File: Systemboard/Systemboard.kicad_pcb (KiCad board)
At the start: 2 copper layers, 194 parts, among them J1 Conn_01x60, J108 Prog BT, J2 Conn_01x02, J3 Conn_01x01, J4 Conn_01x01, J5 PTV112-4420A-A503, Q1 MMBT5551L, Q2 MMBT5551L, Q3 MMBT5551L, Q4 MMBT5551L, Q5 MMBT5551L, U1 INA226, U10 74HC595, U101 ESP32-WROOM-32E, U102 74HC14, U103 TLV73333PDBV, U104 PCM2706CPJTR, U2 LM358, U201 TLV73333PDBV, U202 PCM5102A, U3 J104D2C12VDC.15S, U301 TLV73333PDBV, U4 J104D2C12VDC.15S, U401 74HC14, U5 LM2596S-5, U501 TPA3118D2DAPR, U6 LM2596S-3.3, U7 LM2596S-5, U8 LM2596S-ADJ, U9 LTV-817S, Y101 CSTNE12M0G55A000R0

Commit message: prep board
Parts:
- added REF**: MountingHole_3.2mm_M3, MountingHole:MountingHole_3.2mm_M3, F.Cu at (328.0, 214.0)
- added REF**: MountingHole_3.2mm_M3, MountingHole:MountingHole_3.2mm_M3, F.Cu at (328.0, 254.0)
- moved U501 226.6 mm to (328.0, 234.0)

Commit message: place amp parts
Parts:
- moved Speaker_Front1 376.1 mm to (398.0, 225.6), turned to 90 degrees
- moved Speaker_Rear1 369.3 mm to (392.5, 225.6), turned to 90 degrees
- moved R3 298.8 mm to (388.0, 226.7), turned to -90 degrees
- moved R5 294.9 mm to (388.0, 221.2), turned to -90 degrees
- moved R4 294.1 mm to (388.0, 215.7), turned to -90 degrees
- moved C14 294.0 mm to (385.0, 227.7), turned to 180 degrees
- moved R6 290.8 mm to (388.0, 210.2), turned to -90 degrees
- moved C16 289.8 mm to (385.0, 222.2), turned to 180 degrees
- moved C10 289.5 mm to (376.5, 228.5), turned to -90 degrees
- moved C15 288.6 mm to (385.0, 216.7), turned to 180 degrees
- moved L1 287.5 mm to (370.0, 213.5)
- moved L2 287.3 mm to (370.0, 220.5)
- moved C17 284.8 mm to (385.0, 211.2), turned to 180 degrees
- moved C12 284.7 mm to (376.5, 221.5), turned to -90 degrees
- moved L501 284.6 mm to (370.1, 227.5)
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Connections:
- Speaker_Front1 pad 1: /Speaker_PL -> /Speaker_NL
- Speaker_Front1 pad 2: /Speaker_NL -> /Speaker_PL
- Speaker_Front1 pad 3: /Speaker_PR -> /Speaker_NR
- Speaker_Front1 pad 4: /Speaker_NR -> /Speaker_PR
- Speaker_Rear1 pad 1: /Speaker_PL -> /Speaker_NL
- Speaker_Rear1 pad 2: /Speaker_NL -> /Speaker_PL
- Speaker_Rear1 pad 3: /Speaker_PR -> /Speaker_NR
- Speaker_Rear1 pad 4: /Speaker_NR -> /Speaker_PR

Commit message: user save
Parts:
- removed REF** (x2): MountingHole_3.2mm_M3, MountingHole:MountingHole_3.2mm_M3
- removed U102, U401: 74HC14, Package_SO:SOIC-14_3.9x8.7mm_P1.27mm
- added U11: 74HC14, Package_SO:SOIC-14_3.9x8.7mm_P1.27mm, F.Cu at (143.7, 152.3)
- moved U9 440.9 mm to (489.5, 173.5), turned to -90 degrees
- moved L8 430.1 mm to (478.0, 191.0)
- moved R147 422.2 mm to (492.0, 183.6), turned to 90 degrees
- moved R139 420.4 mm to (489.6, 181.0)
- moved R140 420.4 mm to (489.6, 182.5), turned to 180 degrees
- moved R141 419.5 mm to (490.0, 166.5), turned to 180 degrees
- moved R146 417.6 mm to (487.1, 185.9), turned to 90 degrees
- moved L5 417.1 mm to (466.0, 84.5)
- moved U8 409.8 mm to (478.0, 172.6), turned to 90 degrees
- moved D4 404.8 mm to (467.0, 193.5), turned to -90 degrees
- moved C32 404.7 mm to (490.5, 191.8), turned to -90 degrees
- moved U6 400.1 mm to (466.0, 65.6), turned to 90 degrees
- moved Q4 399.0 mm to (490.0, 186.0)
- moved D2 395.9 mm to (455.5, 87.0), turned to -90 degrees
- moved R148 393.0 mm to (439.2, 17.0), turned to 180 degrees
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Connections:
- C111 pad 1: Net-(U104-VDD) -> /USB DAC/USB_DAC_3V3
- U104 pad 21: Net-(U104-VDD) -> /USB DAC/USB_DAC_3V3

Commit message: Update Systemboard.kicad_pcb
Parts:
- moved C401 312.0 mm to (388.4, -16.3)
- moved C106 310.2 mm to (390.7, -12.2)
- moved R113 308.0 mm to (390.1, -14.2), turned to 180 degrees
- moved C105 306.5 mm to (391.0, -7.62)
- moved R111 304.8 mm to (390.3, -10.2)
- moved R109 301.4 mm to (390.6, -5.59)
- moved C102 295.7 mm to (378.8, -16.0), turned to 180 degrees
- moved C103 295.3 mm to (378.8, -12.2), turned to 180 degrees
- moved C104 294.8 mm to (378.8, -8.38), turned to 180 degrees
- moved R104 293.2 mm to (379.2, -14.0), turned to 180 degrees
- moved R105 292.2 mm to (379.2, -10.2), turned to 180 degrees
- moved R107 291.2 mm to (379.2, -6.35), turned to 180 degrees
- moved U11 290.7 mm to (384.8, -10.2)
- moved J3 283.8 mm to (353.6, -38.4)
- moved J4 280.9 mm to (353.6, -25.4)
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
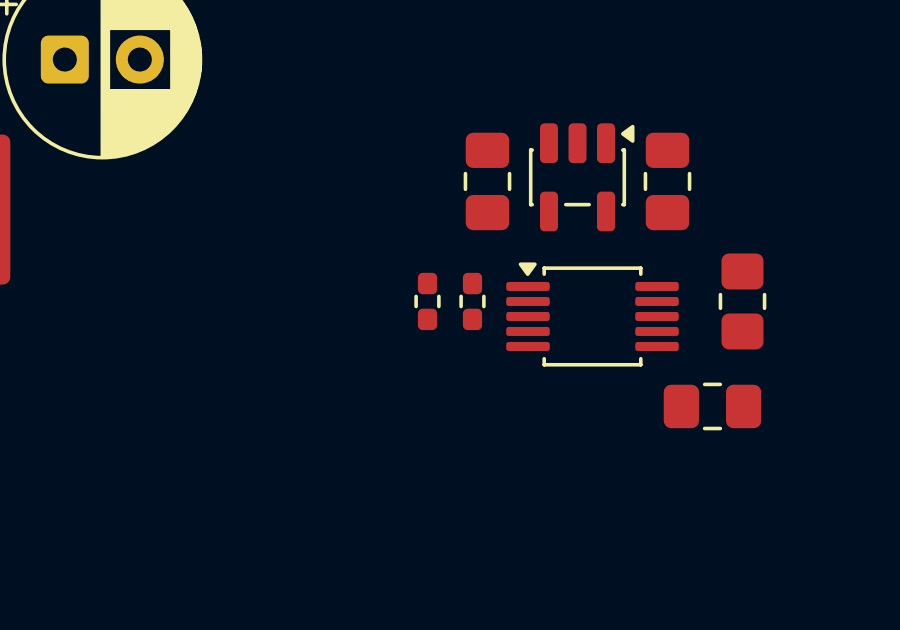
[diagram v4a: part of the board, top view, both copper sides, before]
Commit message: 10k i2c rp down to 4k7
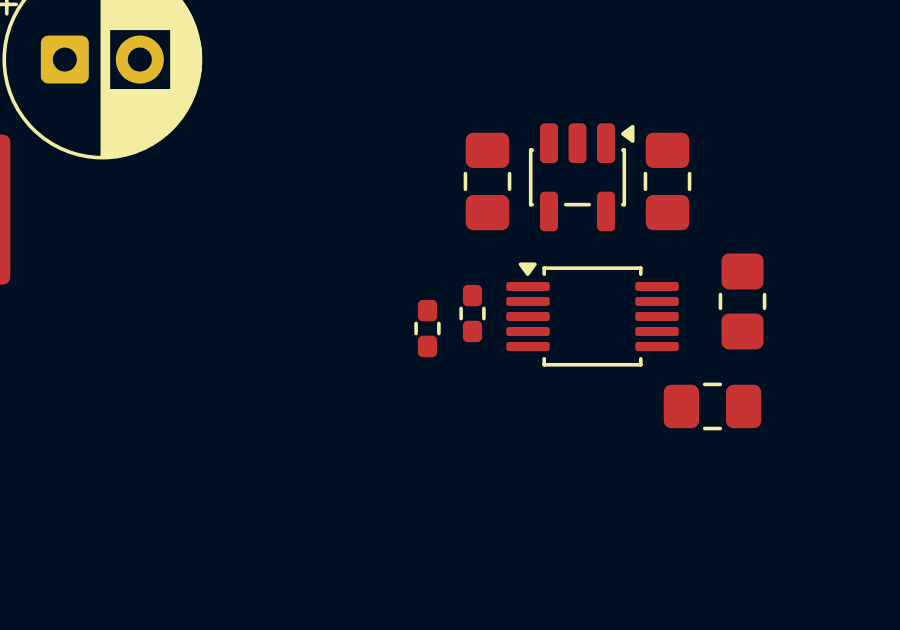
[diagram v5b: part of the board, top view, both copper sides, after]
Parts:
- removed R301, R302: 10k, Resistor_SMD:R_0402_1005Metric_Pad0.72x0.64mm_HandSolder
- added R154: 4k7, Resistor_SMD:R_0402_1005Metric_Pad0.72x0.64mm_HandSolder, F.Cu at (358.0, 67.9)
- added R155: 4k7, Resistor_SMD:R_0402_1005Metric_Pad0.72x0.64mm_HandSolder, F.Cu at (359.5, 67.4)
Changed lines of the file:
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@@
 		)
 	)
+	(footprint "Resistor_SMD:R_0402_1005Metric_Pad0.72x0.64mm_HandSolder"
+		(layer "F.Cu")
+		(at 359.5 67.4025 -90)
+		(descr "Resistor SMD 0402 (1005 Metric), square (rectangular) end terminal, IPC-7351 nominal with elongated pad for handsoldering. (Body size source: IPC-SM-782 page 72, https://www.pcb-3d.com/wordpress/wp-content/uploads/ipc-sm-782a_amendment_1_and_2.pdf)")
+		(tags "resistor handsolder")
+		(property "Reference" "R155"
+			(at 0 -1.17 90)
+			(layer "F.Fab")
+			(effects
+				(font
+					(size 1 1)
+					(thickness 0.15)
+				)
+			)
+		)
+		(property "Value" "4k7"
+			(at 0 1.17 90)
+			(layer "F.Fab")
+			(effects
+				(font
+					(size 1 1)
+					(thickness 0.15)
+				)
+			)
+		)
+		(property "Datasheet" ""
+			(at 0 0 90)
+			(layer "F.Fab")
+			(hide yes)
+			(effects
+				(font
+					(size 1.27 1.27)
+				)
+			)
+		)
+		(property "Description" ""
+			(at 0 0 90)
+			(layer "F.Fab")
+			(hide yes)
+			(effects
+				(font
+					(size 1.27 1.27)
+				)
+			)
+		)
+		(property "KiLib_Generator" "SMD_2terminal_chip_molded"
+			(at 0 0 90)
+			(layer "F.SilkS")
+			(hide yes)
+			(effects
+				(font
+					(size 1 1)
+					(thickness 0.15)
+				)
+			)
+		)
+		(property "DigiKey Part #" "P1.50KLCT-ND"
+			(at 0 0 270)
+			(unlocked yes)
+			(layer "F.Fab")
+			(hide yes)
+			(effects
+				(font
+					(size 1 1)
+					(thickness 0.15)
+				)
+			)
+		)
+		(property "JLCPCB Part #" "C25900"
+			(at 0 0 270)
+			(unlocked yes)
+			(layer "F.Fab")
+			(hide yes)
+			(effects
+				(font
+					(size 1 1)
+					(thickness 0.15)
+				)
+			)
+		)
+		(property ki_fp_filters "R_*")
+		(sheetname "/USB Charger/")
+		(sheetfile "Shunt.kicad_sch")
+		(units
+			(unit
+				(name "A")
+				(pins "1" "2")
+			)
+		)
+		(attr smd)
+		(duplicate_pad_numbers_are_jumpers no)
+		(fp_line
+			(start -0.167621 0.38)
+			(end 0.167621 0.38)
+			(stroke
+				(width 0.12)
+				(type solid)
+			)
+			(layer "F.SilkS")
+		)
+		(fp_line
+			(start -0.167621 -0.38)
+			(end 0.167621 -0.38)
+			(stroke
+				(width 0.12)
+				(type solid)
+			)
+			(layer "F.SilkS")
+		)
+		(fp_rect
+			(start -1.11 -0.47)
+			(end 1.11 0.47)
+			(stroke
+				(width 0.05)
+				(type solid)
+			)
+			(fill no)
+			(layer "F.CrtYd")
+		)
+		(fp_rect
+			(start -0.525 -0.27)
+			(end 0.525 0.27)
+			(stroke
+				(width 0.1)
+				(type solid)
+			)
+			(fill no)
+			(layer "F.Fab")
+		)
+		(fp_text user "${REFERENCE}"
+			(at 0 0 90)
+			(layer "F.Fab")
+			(effects
+				(font
+					(size 0.26 0.26)
+					(thickness 0.04)
+				)
+			)
+		)
+		(pad "1" smd roundrect
+			(at -0.5975 0 270)
+			(size 0.715 0.64)
+			(layers "F.Cu" "F.Mask" "F.Paste")
+			(roundrect_rratio 0.25)
+			(net "Net-(U1-VS)")
+			(pintype "passive")
+		)
+		(pad "2" smd roundrect
+			(at 0.5975 0 270)
+			(size 0.715 0.64)
+			(layers "F.Cu" "F.Mask" "F.Paste")
+			(roundrect_rratio 0.25)
+			(net "/CHARGER_SHUNT_SDA")
+			(pintype "passive")
+		)
+		(embedded_fonts no)
+		(model "${KICAD10_3DMODEL_DIR}/Resistor_SMD.3dshapes/R_0402_1005Metric.step"
+			(offset
+				(xyz 0 0 0)
+			)
+			(scale
+				(xyz 1 1 1)
+			)
+			(rotate
+				(xyz 0 0 0)
+			)
+		)
+	)
 	(footprint "Capacitor_SMD:C_0603_1608Metric_Pad1.08x0.95mm_HandSolder"
 		(layer "F.Cu")
@@
 	(footprint "Resistor_SMD:R_0402_1005Metric_Pad0.72x0.64mm_HandSolder"
 		(layer "F.Cu")
-		(at 359.5 67 90)
+		(at 358 67.9025 -90)
 		(descr "Resistor SMD 0402 (1005 Metric), square (rectangular) end terminal, IPC-7351 nominal with elongated pad for handsoldering. (Body size source: IPC-SM-782 page 72, https://www.pcb-3d.com/wordpress/wp-content/uploads/ipc-sm-782a_amendment_1_and_2.pdf)")
 		(tags "resistor handsolder")
-		(property "Reference" "R302"
+		(property "Reference" "R154"
 			(at 0 -1.17 90)
 			(layer "F.Fab")
@@
 			)
 		)
-		(property "Value" "10k"
+		(property "Value" "4k7"
 			(at 0 1.17 90)
 			(layer "F.Fab")
@@
 			)
 		)
-		(property "DigiKey Part #" "1276-3431-1-ND"
-			(at 0 0 90)
+		(property "DigiKey Part #" "P1.50KLCT-ND"
+			(at 0 0 270)
 			(unlocked yes)
 			(layer "F.Fab")
@@
 			)
 		)
-		(property "JLCPCB Part #" "C25744"
-			(at 0 0 90)
+		(property "JLCPCB Part #" "C25900"
+			(at 0 0 270)
 			(unlocked yes)
 			(layer "F.Fab")
@@
 		(duplicate_pad_numbers_are_jumpers no)
 		(fp_line
-			(start -0.167621 -0.38)
-			(end 0.167621 -0.38)
+			(start -0.167621 0.38)
+			(end 0.167621 0.38)
 			(stroke
 				(width 0.12)
@@
 		)
 		(fp_line
-			(start -0.167621 0.38)
-			(end 0.167621 0.38)
+			(start -0.167621 -0.38)
+			(end 0.167621 -0.38)
 			(stroke
 				(width 0.12)
@@
 		)
 		(pad "1" smd roundrect
-			(at -0.5975 0 90)
+			(at -0.5975 0 270)
 			(size 0.715 0.64)
 			(layers "F.Cu" "F.Mask" "F.Paste")
 			(roundrect_rratio 0.25)
-			(net "/CHARGER_SHUNT_SDA")
+			(net "Net-(U1-VS)")
 			(pintype "passive")
 		)
 		(pad "2" smd roundrect
-			(at 0.5975 0 90)
+			(at 0.5975 0 270)
 			(size 0.715 0.64)
 			(layers "F.Cu" "F.Mask" "F.Paste")
 			(roundrect_rratio 0.25)
-			(net "Net-(U1-VS)")
+			(net "/CHARGER_SHUNT_SCL")
 			(pintype "passive")
 		)
@@
 		)
 	)
-	(footprint "Resistor_SMD:R_0402_1005Metric_Pad0.72x0.64mm_HandSolder"
-		(layer "F.Cu")
-		(at 358 67 90)
-		(descr "Resistor SMD 0402 (1005 Metric), square (rectangular) end terminal, IPC-7351 nominal with elongated pad for handsoldering. (Body size source: IPC-SM-782 page 72, https://www.pcb-3d.com/wordpress/wp-content/uploads/ipc-sm-782a_amendment_1_and_2.pdf)")
-		(tags "resistor handsolder")
-		(property "Reference" "R301"
-			(at 0 -1.17 90)
-			(layer "F.Fab")
-			(effects
-				(font
-					(size 1 1)
-					(thickness 0.15)
-				)
-			)
-		)
-		(property "Value" "10k"
-			(at 0 1.17 90)
-			(layer "F.Fab")
-			(effects
-				(font
-					(size 1 1)
-					(thickness 0.15)
-				)
-			)
-		)
-		(property "Datasheet" ""
-			(at 0 0 90)
-			(layer "F.Fab")
-			(hide yes)
-			(effects
-				(font
-					(size 1.27 1.27)
-				)
-			)
-		)
-		(property "Description" ""
-			(at 0 0 90)
-			(layer "F.Fab")
-			(hide yes)
-			(effects
-				(font
-					(size 1.27 1.27)
-				)
-			)
-		)
-		(property "KiLib_Generator" "SMD_2terminal_chip_molded"
-			(at 0 0 90)
-			(layer "F.SilkS")
-			(hide yes)
-			(effects
-				(font
-					(size 1 1)
-					(thickness 0.15)
-				)
-			)
-		)
-		(property "DigiKey Part #" "1276-3431-1-ND"
-			(at 0 0 90)
-			(unlocked yes)
-			(layer "F.Fab")
-			(hide yes)
-			(effects
-				(font
-					(size 1 1)
-					(thickness 0.15)
-				)
-			)
-		)
-		(property "JLCPCB Part #" "C25744"
-			(at 0 0 90)
-			(unlocked yes)
-			(layer "F.Fab")
-			(hide yes)
-			(effects
-				(font
-					(size 1 1)
-					(thickness 0.15)
-				)
-			)
-		)
-		(property ki_fp_filters "R_*")
-		(sheetname "/USB Charger/")
-		(sheetfile "Shunt.kicad_sch")
-		(units
-			(unit
-				(name "A")
-				(pins "1" "2")
-			)
-		)
-		(attr smd)
-		(duplicate_pad_numbers_are_jumpers no)
-		(fp_line
-			(start -0.167621 -0.38)
-			(end 0.167621 -0.38)
-			(stroke
-				(width 0.12)
-				(type solid)
-			)
-			(layer "F.SilkS")
-		)
-		(fp_line
-			(start -0.167621 0.38)
-			(end 0.167621 0.38)
-			(stroke
-				(width 0.12)
-				(type solid)
-			)
-			(layer "F.SilkS")
-		)
-		(fp_rect
-			(start -1.11 -0.47)
-			(end 1.11 0.47)
-			(stroke
-				(width 0.05)
-				(type solid)
-			)
-			(fill no)
-			(layer "F.CrtYd")
-		)
-		(fp_rect
-			(start -0.525 -0.27)
-			(end 0.525 0.27)
-			(stroke
-				(width 0.1)
-				(type solid)
-			)
-			(fill no)
-			(layer "F.Fab")
-		)
-		(fp_text user "${REFERENCE}"
-			(at 0 0 90)
-			(layer "F.Fab")
-			(effects
-				(font
-					(size 0.26 0.26)
-					(thickness 0.04)
-				)
-			)
-		)
-		(pad "1" smd roundrect
-			(at -0.5975 0 90)
-			(size 0.715 0.64)
-			(layers "F.Cu" "F.Mask" "F.Paste")
-			(roundrect_rratio 0.25)
-			(net "/CHARGER_SHUNT_SCL")
-			(pintype "passive")
-		)
-		(pad "2" smd roundrect
-			(at 0.5975 0 90)
-			(size 0.715 0.64)
-			(layers "F.Cu" "F.Mask" "F.Paste")
-			(roundrect_rratio 0.25)
-			(net "Net-(U1-VS)")
-			(pintype "passive")
-		)
-		(embedded_fonts no)
-		(model "${KICAD10_3DMODEL_DIR}/Resistor_SMD.3dshapes/R_0402_1005Metric.step"
-			(offset
-				(xyz 0 0 0)
-			)
-			(scale
-				(xyz 1 1 1)
-			)
-			(rotate
-				(xyz 0 0 0)
-			)
-		)
-	)
 	(footprint "Inductor_SMD:L_Wuerth_HCI-1365"
 		(layer "F.Cu")
@@
 	(group ""
 		(members "0671811d-7f08-4c1d-81d4-38e3dc55d66d" "0f73532c-b3b8-4385-ae73-0066597dcadd"
-			"6a10997a-816c-4f80-b0a6-284202d63ef8" "7e83e4d8-2f0d-4ac9-8ba6-c5590b1e6896"
-			"95b34e39-395b-4c56-b277-22aec886abab" "dcc9216a-1377-409a-a669-ddba4ebb8e42"
-			"e2b027e4-f4ff-4f89-9722-64542c4b94c4" "f8c646f4-75a6-4f5e-8c63-c4cedc80619e"
+			"42c5646a-5f9c-47d7-b6f5-3f1816dfbf8e" "6a10997a-816c-4f80-b0a6-284202d63ef8"
+			"7ecd18b1-39cd-4eab-950f-5b2c966cd6a4" "95b34e39-395b-4c56-b277-22aec886abab"
+			"dcc9216a-1377-409a-a669-ddba4ebb8e42" "f8c646f4-75a6-4f5e-8c63-c4cedc80619e"
 		)
 	)

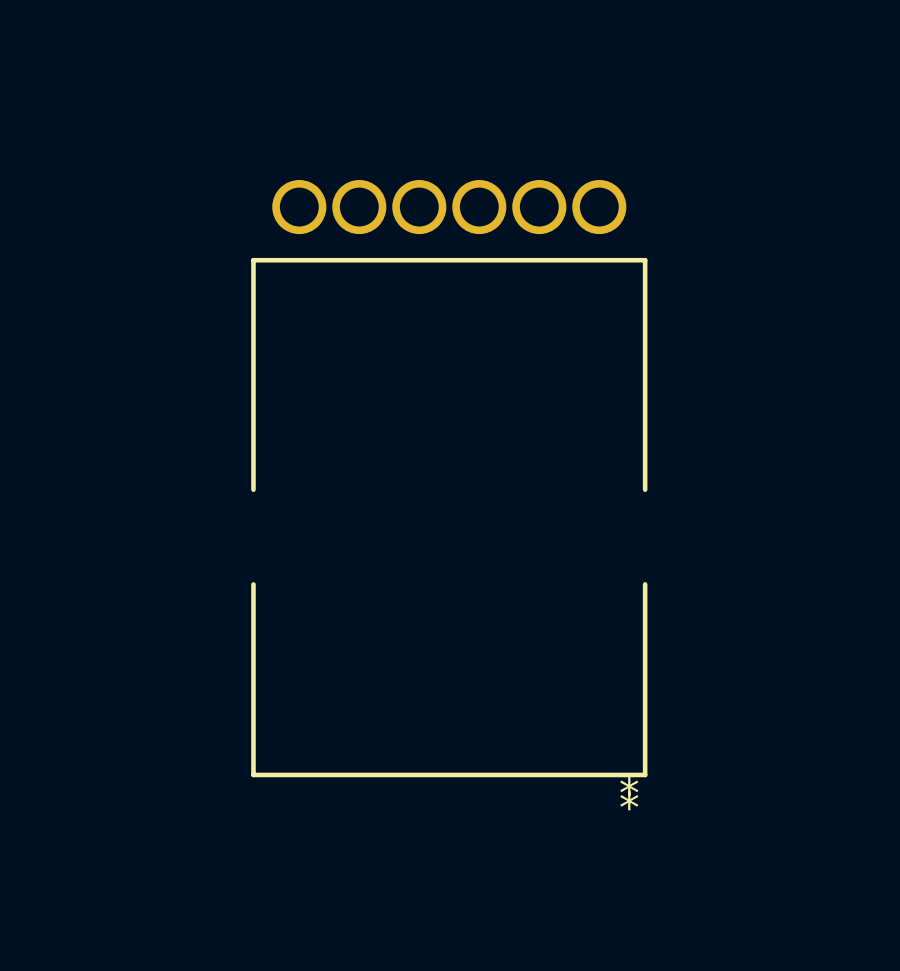
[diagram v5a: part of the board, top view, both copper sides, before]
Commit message: remove circular potentiometer
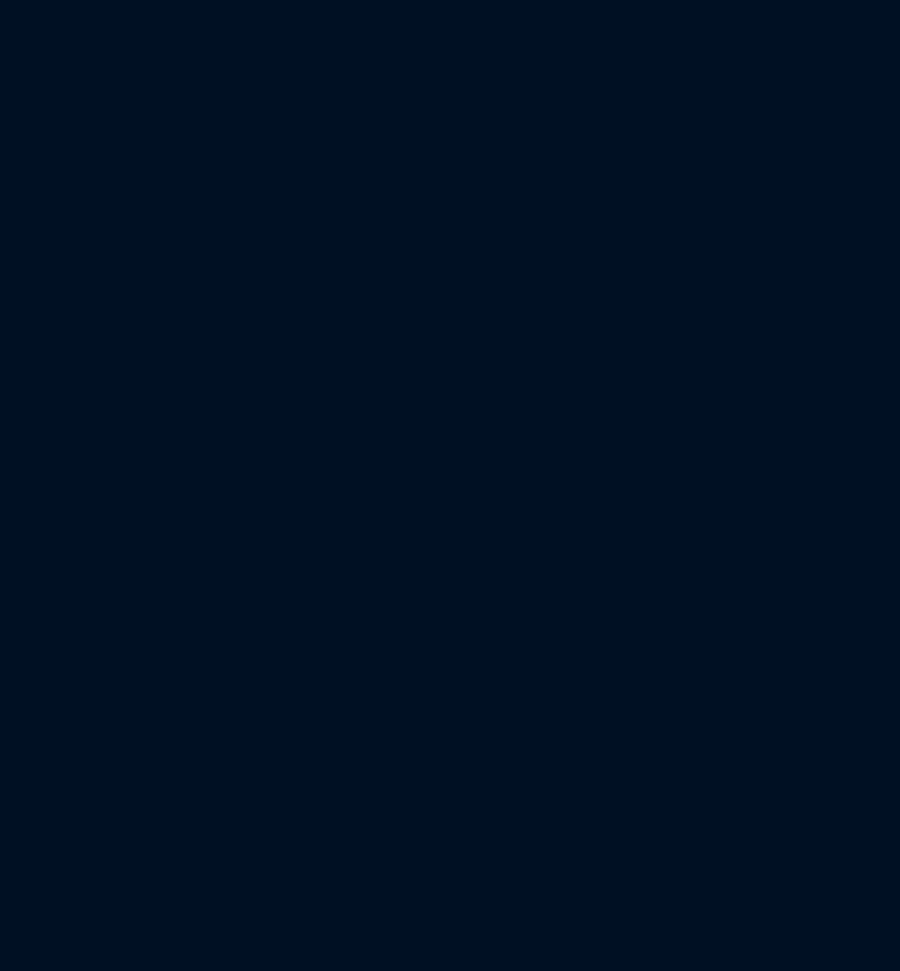
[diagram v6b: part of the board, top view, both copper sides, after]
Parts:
- removed J5: PTV112-4420A-A503, External_Parts:CONN_A503
